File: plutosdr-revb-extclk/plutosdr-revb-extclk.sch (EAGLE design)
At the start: 26 parts

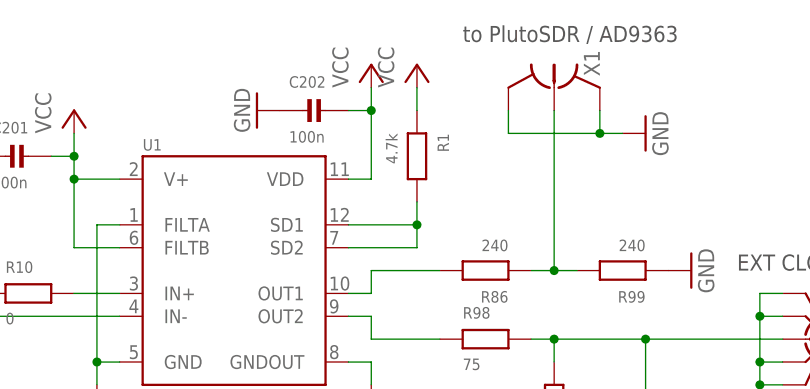
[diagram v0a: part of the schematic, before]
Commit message: plutosdr-revb-extclk: don't shut-down LTC via SD1/SD2
In the original PlutoSDR RevC or higher, there's a BSS138 FET
that [optionally] pulls low the SD1/SD2 pins in order to activate
the external clock input.

In this circuit, we don't have GPIO control but permanently enable
the LTC.

Related: OS#5892
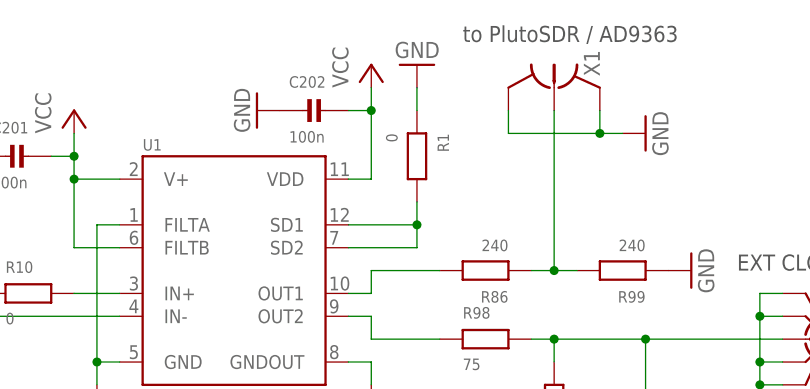
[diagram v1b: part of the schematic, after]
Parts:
- R1: value 4.7k -> 0
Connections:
- net GND: now also R1.1
- net VCC: no longer R1.1
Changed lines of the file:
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@@
 <part name="P+1" library="supply1" deviceset="VCC" device=""/>
 <part name="P+2" library="supply1" deviceset="VCC" device=""/>
-<part name="R1" library="rc-sysmocom" deviceset="RESISTOR" device="_0603" value="4.7k"/>
-<part name="P+3" library="supply1" deviceset="VCC" device=""/>
+<part name="R1" library="rc-sysmocom" deviceset="RESISTOR" device="_0603" value="0"/>
 <part name="C205" library="rc-sysmocom" deviceset="CAP_CERAMIC" device="0603" value="10n"/>
 <part name="C180" library="rc-sysmocom" deviceset="CAP_CERAMIC" device="0603" value="10n"/>
@@
 <part name="GND17" library="supply1" deviceset="GND" device=""/>
 <part name="GND18" library="supply1" deviceset="GND" device=""/>
+<part name="GND19" library="supply1" deviceset="GND" device=""/>
 </parts>
 <sheets>
@@
 <instance part="P+2" gate="VCC" x="99.06" y="175.26"/>
 <instance part="R1" gate="G$1" x="104.14" y="165.1" rot="R270"/>
-<instance part="P+3" gate="VCC" x="104.14" y="175.26"/>
 <instance part="C205" gate="G$1" x="119.38" y="124.46" rot="R90"/>
 <instance part="C180" gate="G$1" x="48.26" y="127" rot="R90"/>
@@
 <instance part="GND17" gate="1" x="53.34" y="165.1" rot="R270"/>
 <instance part="GND18" gate="1" x="86.36" y="170.18" rot="R270"/>
+<instance part="GND19" gate="1" x="104.14" y="175.26" rot="R180"/>
 </instances>
 <busses>
@@
 <pinref part="GND18" gate="1" pin="GND"/>
 </segment>
+<segment>
+<pinref part="R1" gate="G$1" pin="1"/>
+<wire x1="104.14" y1="172.72" x2="104.14" y2="170.18" width="0.1524" layer="91"/>
+<pinref part="GND19" gate="1" pin="GND"/>
+</segment>
 </net>
 <net name="N$1" class="0">
@@
 </segment>
 <segment>
-<pinref part="R1" gate="G$1" pin="1"/>
-<pinref part="P+3" gate="VCC" pin="VCC"/>
-<wire x1="104.14" y1="172.72" x2="104.14" y2="170.18" width="0.1524" layer="91"/>
-</segment>
-<segment>

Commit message: plutosdr-revb-extclk: Fix capacitor footprints
* Always use _0603 and not 0603 (oversized)
* 1uF can be 0603, only 10uF should be 0805

Related: OS#5892
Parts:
- C179, C180, C201, C202, C205: device rc-sysmocom:CAP_CERAMIC0603 -> rc-sysmocom:CAP_CERAMIC_0603
- C196, C200: device rc-sysmocom:CAP_CERAMIC_0805 -> rc-sysmocom:CAP_CERAMIC_0603
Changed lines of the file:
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@@
 <part name="P+2" library="supply1" deviceset="VCC" device=""/>
 <part name="R1" library="rc-sysmocom" deviceset="RESISTOR" device="_0603" value="0"/>
-<part name="C205" library="rc-sysmocom" deviceset="CAP_CERAMIC" device="0603" value="10n"/>
-<part name="C180" library="rc-sysmocom" deviceset="CAP_CERAMIC" device="0603" value="10n"/>
-<part name="C179" library="rc-sysmocom" deviceset="CAP_CERAMIC" device="0603" value="10n"/>
-<part name="C201" library="rc-sysmocom" deviceset="CAP_CERAMIC" device="0603" value="100n"/>
-<part name="C202" library="rc-sysmocom" deviceset="CAP_CERAMIC" device="0603" value="100n"/>
+<part name="C205" library="rc-sysmocom" deviceset="CAP_CERAMIC" device="_0603" value="10n"/>
+<part name="C180" library="rc-sysmocom" deviceset="CAP_CERAMIC" device="_0603" value="10n"/>
+<part name="C179" library="rc-sysmocom" deviceset="CAP_CERAMIC" device="_0603" value="10n"/>
+<part name="C201" library="rc-sysmocom" deviceset="CAP_CERAMIC" device="_0603" value="100n"/>
+<part name="C202" library="rc-sysmocom" deviceset="CAP_CERAMIC" device="_0603" value="100n"/>
 <part name="D7" library="laforge" deviceset="0603ESDA-TR" device=""/>
 <part name="D8" library="laforge" deviceset="0603ESDA-TR" device=""/>
@@
 <part name="GND11" library="supply1" deviceset="GND" device=""/>
 <part name="GND12" library="supply1" deviceset="GND" device=""/>
-<part name="C196" library="rc-sysmocom" deviceset="CAP_CERAMIC" device="_0805" value="1u"/>
-<part name="C200" library="rc-sysmocom" deviceset="CAP_CERAMIC" device="_0805" value="1u"/>
+<part name="C196" library="rc-sysmocom" deviceset="CAP_CERAMIC" device="_0603" value="1u"/>
+<part name="C200" library="rc-sysmocom" deviceset="CAP_CERAMIC" device="_0603" value="1u"/>
 <part name="GND13" library="supply1" deviceset="GND" device=""/>
 <part name="GND14" library="supply1" deviceset="GND" device=""/>

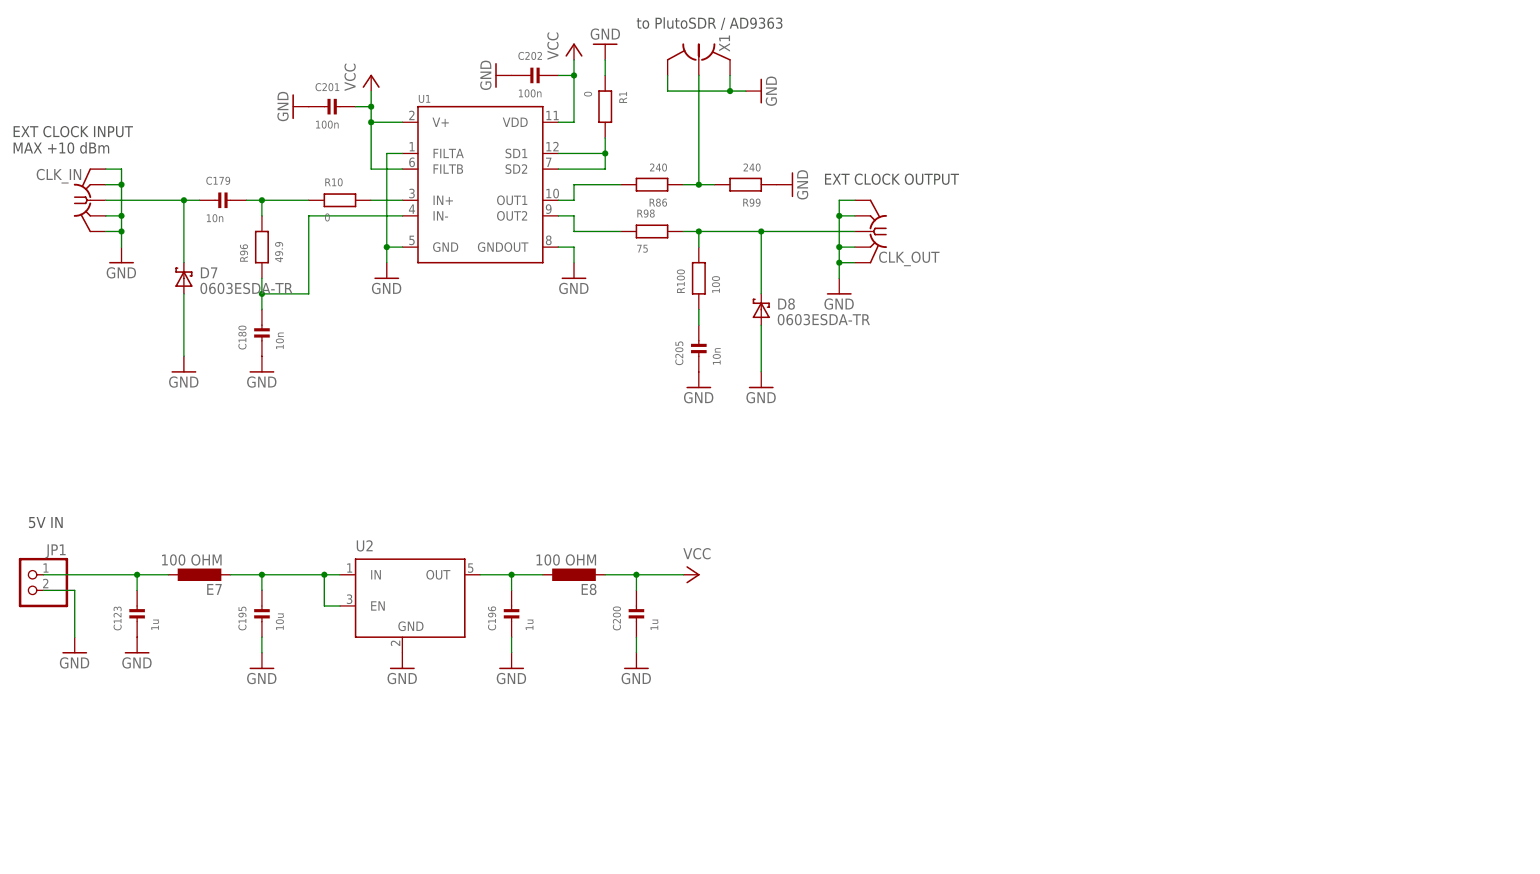
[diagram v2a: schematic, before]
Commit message: WIP: plutosdr-revb-extclk: support switching back to original 40MHz XO
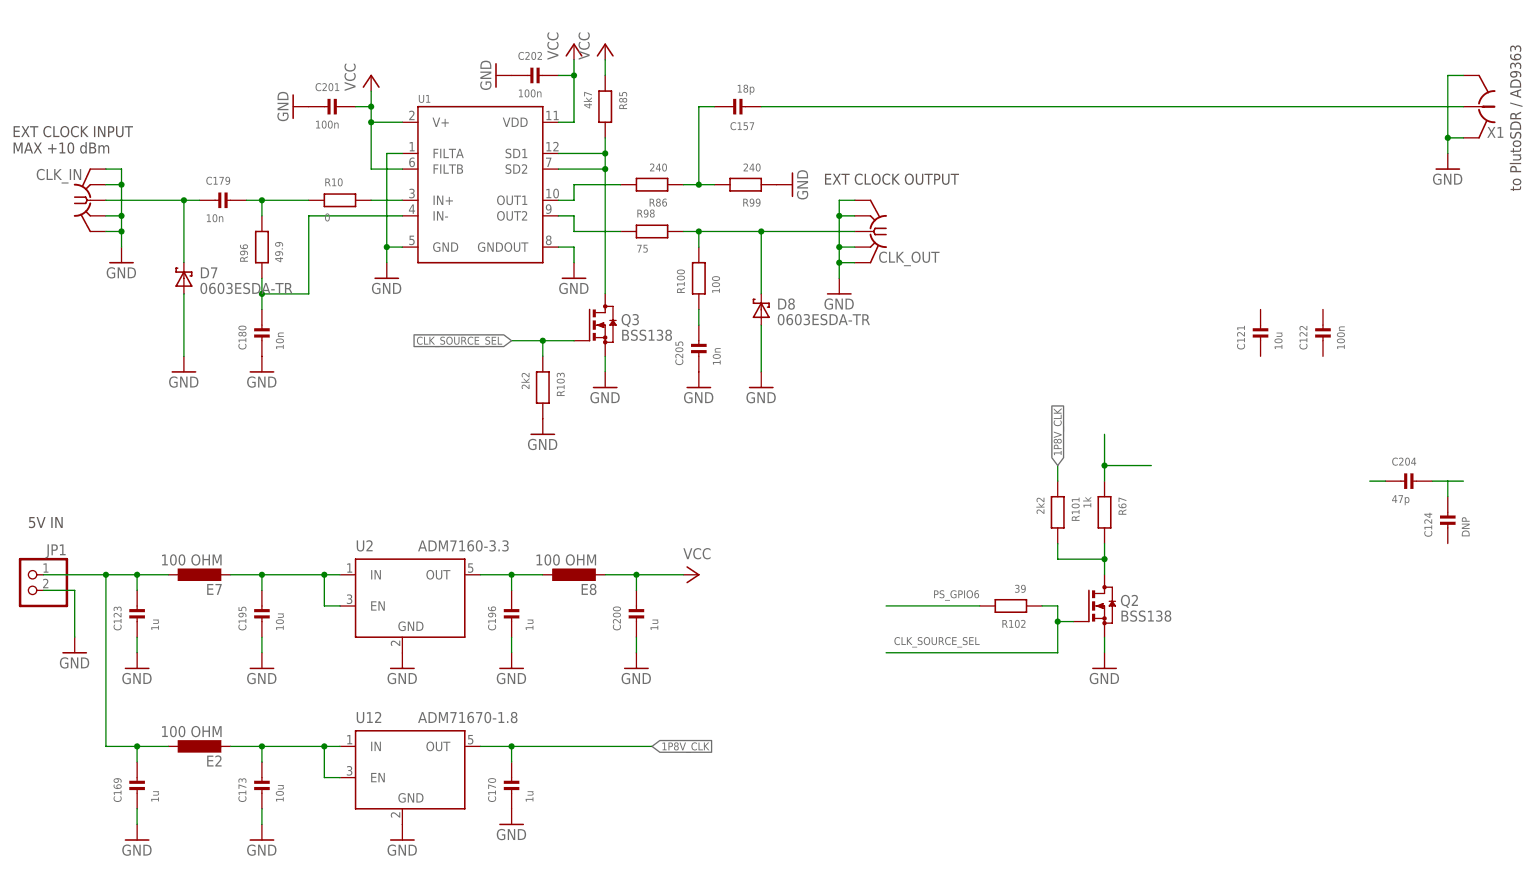
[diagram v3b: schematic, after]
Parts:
- added C121, C173: 10u, rc-sysmocom:CAP_CERAMIC_0805
- added C122: 100n, rc-sysmocom:CAP_CERAMIC_0603
- added C124: DNP, rc-sysmocom:CAP_CERAMIC_0603
- added C157: 18p, rc-sysmocom:CAP_CERAMIC_0603
- added C169, C170: 1u, rc-sysmocom:CAP_CERAMIC_0603
- added C204: 47p, rc-sysmocom:CAP_CERAMIC_0603
- added E2: 100 OHM, rc-sysmocom:INDUCTOR0805
- added Q2, Q3: BSS138, transistor-small-signal:BSS123
- added R101, R103: 2k2, rc-sysmocom:RESISTOR_0603
- added R102: 39, rc-sysmocom:RESISTOR_0603
- added R67: 1k, rc-sysmocom:RESISTOR_0603
- added U12: ADM71670-1.8, ldo:LDO_FIXED_EN-ADM7160AUJZ
- R85: value 0 -> 4k7
- U2: value (none) -> ADM7160-3.3
- renumbered R1 to R85
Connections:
- new net 1P8V_CLK: C170.2, R101.1, U12.OUT
- new net CLK_SOURCE_SEL: Q2.G, Q3.G, R102.1, R103.1
- new net N$11: C173.2, E2.2, U12.EN, U12.IN
- new net N$12: Q2.D, R101.2, R67.2
- new net N$13: R67.1
- new net N$14: C124.2, C204.2
- new net N$15: C204.1
- new net N$16: C157.1, X1.1
- new net PS_GPIO6: R102.2
- net 5V_IN: now also C169.2, E2.1
- net GND: now also C169.1, C170.1, C173.1, Q2.S, Q3.S, R103.2, U12.GND; no longer R85.1
- net N$1: now also C157.2; no longer X1.1
- net N$7: now also Q3.D
- net VCC: now also R85.1
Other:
- moved on the sheet: X1
